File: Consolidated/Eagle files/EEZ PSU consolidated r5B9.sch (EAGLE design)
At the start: 534 parts, among them IC1 LTC3864EMSE#PBF, IC10 REF5025AIDG4, IC11 DAC8552IDGKTG4, IC12 ADG465SOT-23, IC13 TS5A9411DCKT, IC14 ADS1120IPWR, IC15 LP339D, IC16 LM25575MH/NOPB, IC17 TPD4E002DRLR, IC18 TPD2E001DZDR, IC19 ADUM3160BRWZ, IC2 MC79L05, IC20 TLC5925IDBQR, IC21 Si8641EC-B-IS1, IC22 SI8651EC-B-IS1, IC23 SI8651EC-B-IS1, IC24 LD1117ADT33TR, IC25 Si8641EC-B-IS1, IC26 PCA21125T/Q900/1,1, IC27 AT25256B-SSHL-B, IC28 W5500, IC29 BC857BS, IC3 MC78L05, IC30 TLC555, IC31 SN74LVC2G08DCTR, IC32 TPS3705-33D, IC33 SN74LV1T34DBVR, IC34 SN74LVC2G02DCTR, IC4 LM5574MTX/NOPB, IC5 LP2951SO8, IC6 TL072D, IC7 TL072D, IC8 OP27GSZ, IC9 MCP23S08-E/SO, J1 BS-244DSM-R, J2 BS-244DSM-G, J3 BS-244DSM-B, J4 BS-244DSM-R, J5 BS-244DSM-B, Q1 SUD19P06-60, Q10 MMBT5401, Q11 MMBT5401, Q12 MMBT5551, Q13 MMBT5551, Q14 BSS84P, Q15 2N7002, Q16 MMBT5551, Q17 MMBT5401, Q18 MMBT5551, Q19 MMBT5551, Q2 MMBT5401, Q20 BTA26-600, Q21 BTA26-600, Q22 IRLL014N, Q23 IRLML2246TRPBF, Q24 IRLML2246TRPBF, Q25 IRLML2246TRPBF, Q26 IRLML2246TRPBF, Q27 2N7002, Q28 IRLML2246TRPBF, Q29 2N7002, Q3 2N7002, Q30 2N7002, Q4 IRFP250N, Q5 BC857C, Q6 BC846C, Q7 BCP56-16.115, Q8 IRFR5410, Q9 BCP56-16.115, SW1 A101SYCQ04, SW2 1301.9316, X1 39303035, X10 826629-5, X11 2411-01, X12 MC000006, X13 TSW-113-07-F-D, X14 MC000005, X15 TSW-113-07-F-D, X16 09185067324, X17 22-23-2021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

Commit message: C39 marked as n.c.
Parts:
- C39: value 2u2 -> n.c.
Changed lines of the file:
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@@
 <part name="D10" library="EEZ_Lib1" deviceset="SCHOTTKY" device="SOD123" value="DFLS1100-7"/>
 <part name="C31" library="rcl" deviceset="C-EU" device="C1206" value="1u/100V"/>
-<part name="C39" library="rcl" deviceset="C-EU" device="C0805" value="2u2">
+<part name="C39" library="rcl" deviceset="C-EU" device="C0805" value="n.c.">
 <variant name="Farnell" value="2320829"/>
 <variant name="TME" value="CL21B225KAFNNNG "/>

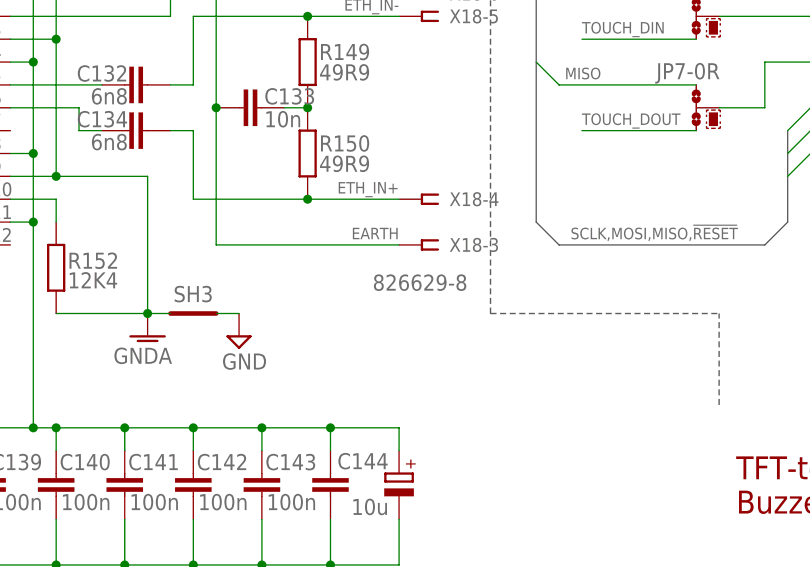
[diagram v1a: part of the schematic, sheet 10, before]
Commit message: X18 type changed
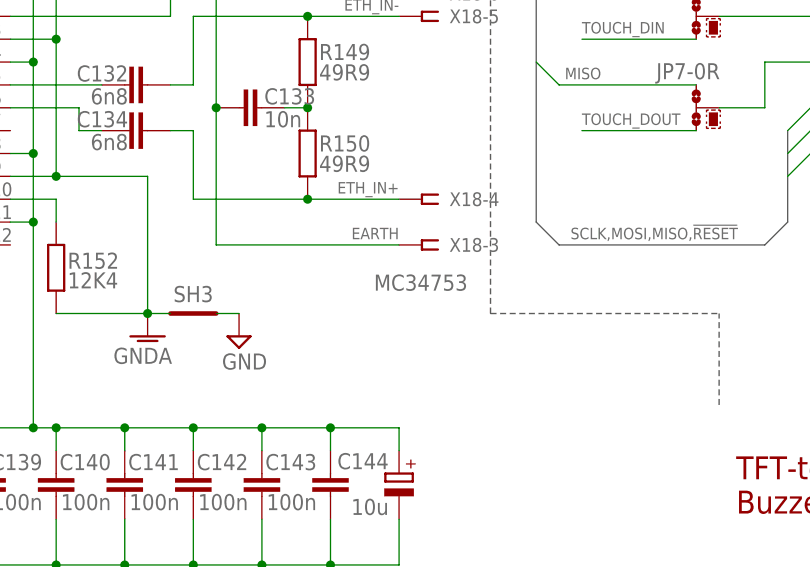
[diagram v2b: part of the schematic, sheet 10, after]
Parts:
- X18: value 826629-8 -> MC34753
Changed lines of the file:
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@@
 <part name="OK3" library="EEZ_Lib1" deviceset="HCPL-181" device=""/>
 <part name="R159" library="rcl" deviceset="R-EU_" device="R0805" value="1K8"/>
-<part name="X18" library="con-samtec" deviceset="SSW-108-02-S-S" device="" value="826629-8">
+<part name="X18" library="con-samtec" deviceset="SSW-108-02-S-S" device="" value="MC34753">
 <attribute name="MPN" value="SSW-108-02-S-S"/>
 <attribute name="OC_NEWARK" value="11P9448"/>

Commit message: R97 and R102 values swapped
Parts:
- R102: value 5K6 -> 4K7
- R97: value 4K7 -> 5K6
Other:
- note added: "+0.275V"
- note added: "+5.18V @ Vout=+5V"
- note added: "+5.19V @ Vout=+5V"
- note added: "-2.72V"
- note removed: "+0.22V"
- note removed: "-2.27V"
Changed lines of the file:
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@@
 <part name="C73" library="rcl" deviceset="C-EU" device="C0603" value="100n"/>
 <part name="FRAME5" library="frames" deviceset="DINA4_L" device=""/>
-<part name="R102" library="rcl" deviceset="R-EU_" device="R0805" value="5K6"/>
+<part name="R102" library="rcl" deviceset="R-EU_" device="R0805" value="4K7"/>
 <part name="R94" library="rcl" deviceset="R-EU_" device="R0805" value="2K2"/>
 <part name="R92" library="rcl" deviceset="R-EU_" device="R0805" value="5K6"/>
@@
 <part name="SUPPLY4" library="supply2" deviceset="GND" device="" value="PGND"/>
 <part name="SUPPLY22" library="supply2" deviceset="GND" device="" value="PGND"/>
-<part name="R97" library="rcl" deviceset="R-EU_" device="R0805" value="4K7"/>
+<part name="R97" library="rcl" deviceset="R-EU_" device="R0805" value="5K6"/>
 <part name="SUPPLY1" library="supply2" deviceset="GND" device="" value="PGND"/>
 <part name="SUPPLY2" library="supply2" deviceset="-9V" device=""/>
@@
 <plain>
 <text x="7.62" y="172.72" size="1.778" layer="97" rot="MR180">Constant Voltage (CV) and Constant Current (CC) mode indicator</text>
-<text x="87.63" y="144.145" size="1.27" layer="100" rot="MR180">+0.22V</text>
+<text x="87.63" y="144.145" size="1.27" layer="100" rot="MR180">+0.275V</text>
 <text x="164.465" y="28.575" size="2.54" layer="94" font="vector">CC/CV indicators, Sense error detection</text>
 <polygon width="0.1524" layer="101">
 </polygon>
-<text x="88.265" y="118.745" size="1.27" layer="100" rot="MR180">-2.27V</text>
+<text x="88.265" y="118.745" size="1.27" layer="100" rot="MR180">-2.72V</text>
 <text x="2.54" y="7.62" size="1.778" layer="94">Licensed under the TAPR Open Hardware License (www.tapr.org/OHL)</text>
 <text x="2.54" y="2.54" size="1.778" layer="94">Repository: https://github.com/eez-open</text>
@@
 <wire x1="7.62" y1="76.835" x2="134.62" y2="76.835" width="0.1524" layer="97" style="shortdash"/>
 <wire x1="134.62" y1="76.835" x2="259.08" y2="76.835" width="0.1524" layer="97" style="shortdash"/>
+<text x="57.15" y="139.065" size="1.27" layer="100" rot="MR180">+5.19V @ Vout=+5V</text>
+<text x="22.225" y="142.875" size="1.27" layer="100" rot="MR180">+5.18V @ Vout=+5V</text>
 </plain>
 <instances>

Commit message: new BOM, added RS and DigiKeyne
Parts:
- C1, C2, C3: value 100n -> 4n7/100V
- C105, C108, C110, C112: value 10n -> 4n7/200V
- C106, C111: value UPW1J150MED -> EEEFK1J220P
- C47, C51: value 1n -> 2n2
- Q1: value SUD19P06-60 -> IRFR5305
- X5: value 09185067324 -> 09185107324
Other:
- note added: "15K / 16K"
- note added: "20K / 22K"
- note added: "Make this correction to enable remote voltage programming!"
- note added: "Note 1.1: Possible alternative AUIRFR5305, SUD19P06-60, SPD30P06P or other with similar or lower input capacitance"
- note added: "Note 1.4: Install 0R only if 100% Duty cycle feature is not needed (do not mount Q3 in that case)"
- note added: "Note 3.2: Place for optional TVS (its primary position is on the Arduino shield board)"
- note added: "R47, R57 / ext.range"
- note removed: "+5.18V @ Vout=+5V"
- note removed: "+5.19V @ Vout=+5V"
- note removed: "15K"
- note removed: "20K"
- note removed: "DC input option"
- note removed: "IRFP250N"
- note removed: "IRFP260N"
- note removed: "Note 1.1: D1-D5, L2 and Q1 requires thermal bridge to the external heatsink. See layer 114 on Board editor for an example."
- note removed: "Note 1.4: Install 0R only if 100% Duty cycle feature is not needed"
- note removed: "Note 3.2: Place for optional TVS (primary place is the Arduino shield board)"
- note removed: "Q4"
- note removed: "R47, R57"
- moved on the sheet: C1, C10, C11, C12, C13, C14, C15, C16, C17, C18, C19, C20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

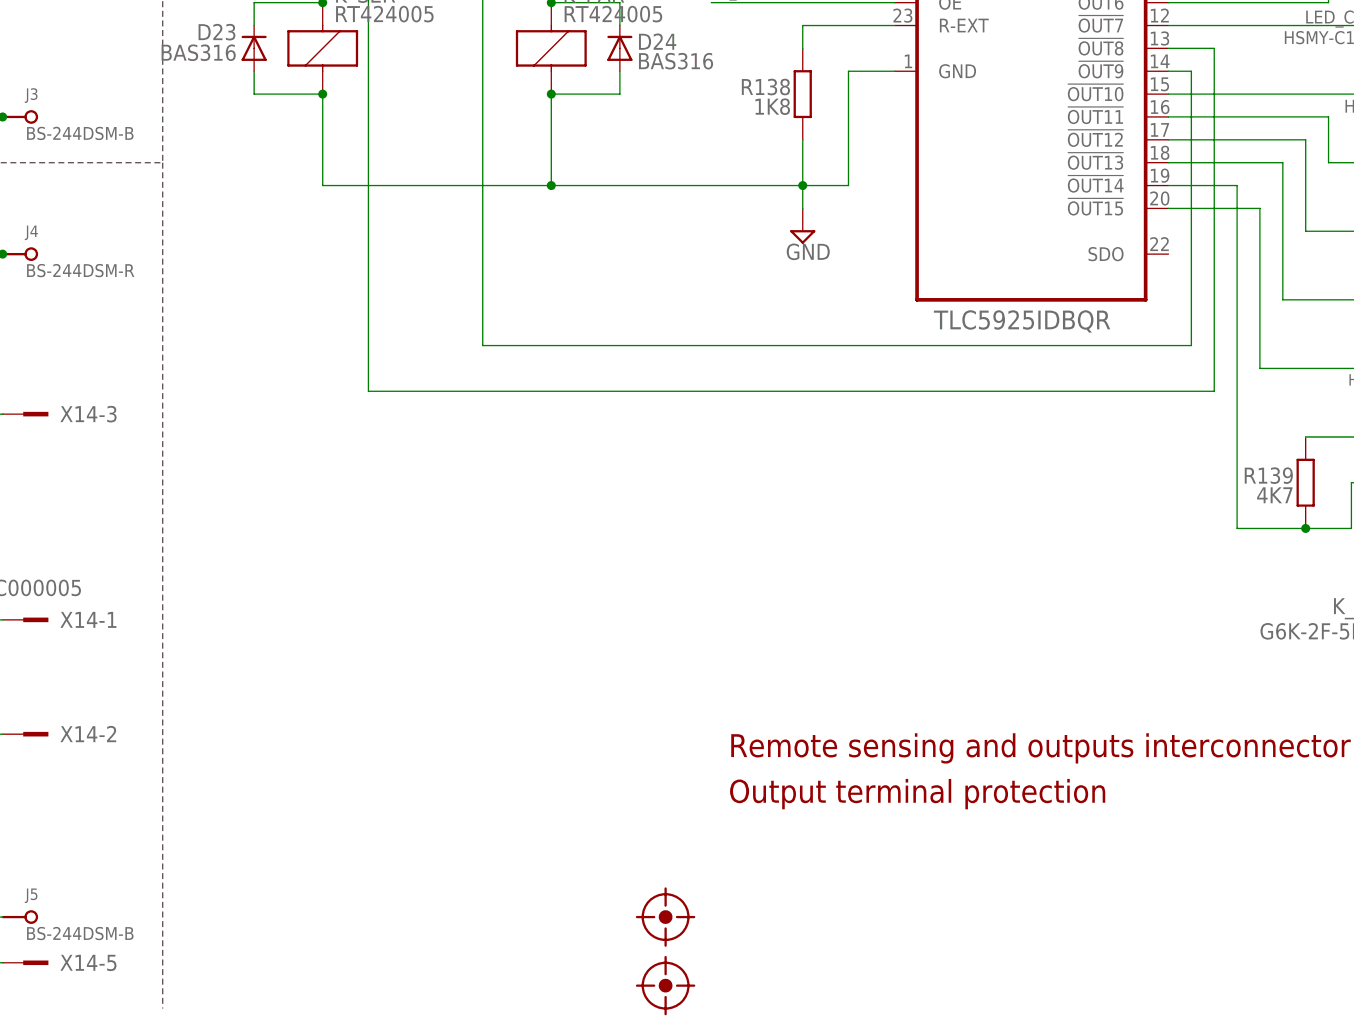
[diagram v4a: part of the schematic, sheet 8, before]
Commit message: Changed wrong designators in schematics on page 3, 6 and 8
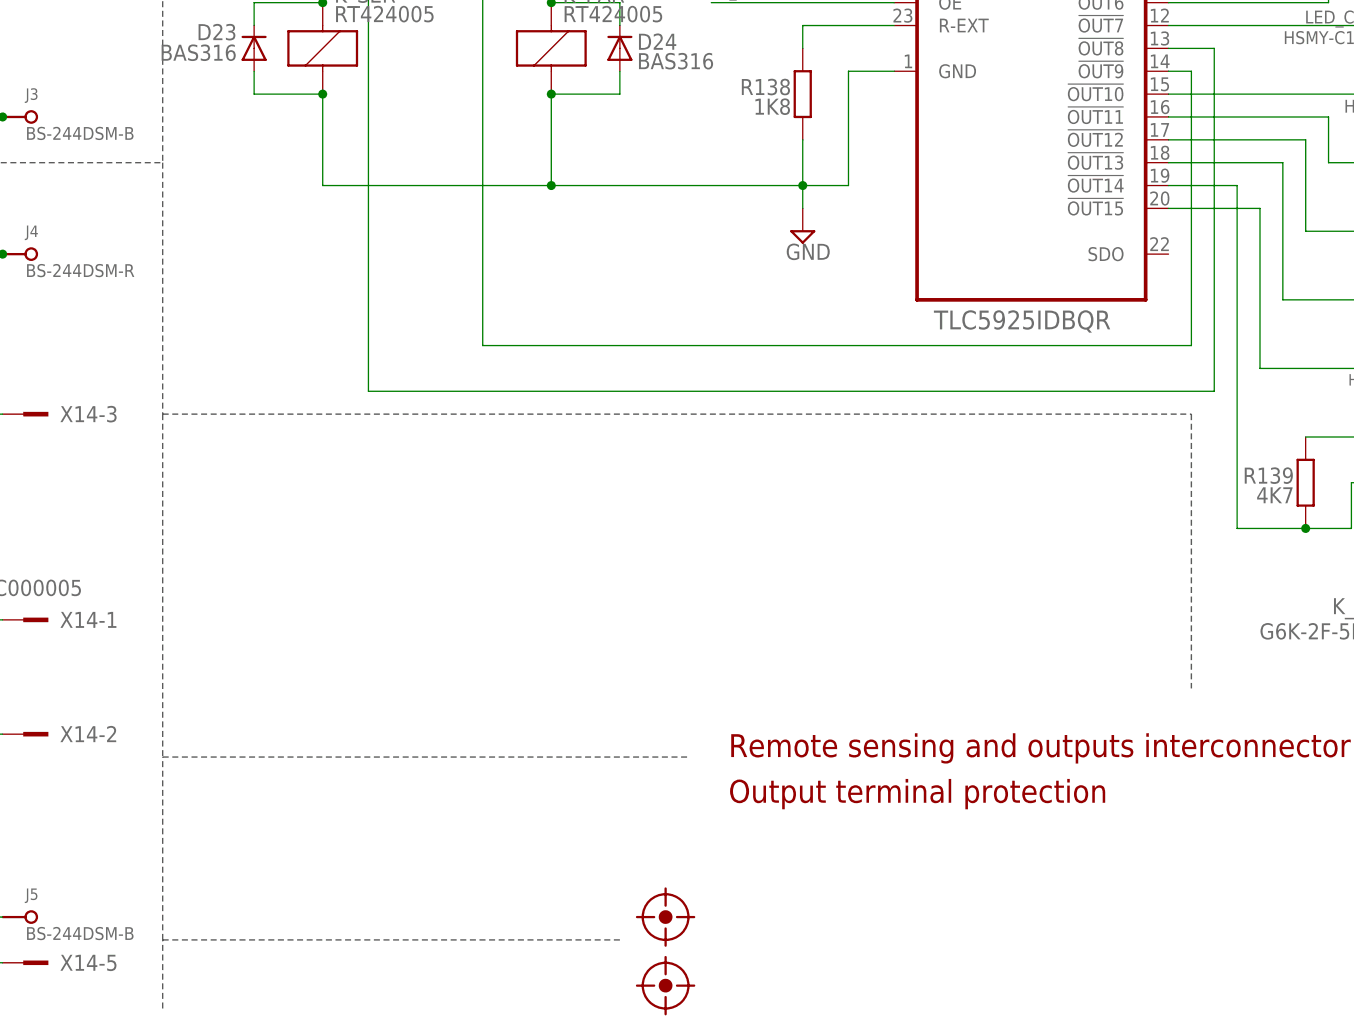
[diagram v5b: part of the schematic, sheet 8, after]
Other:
- note added: "(Rout1, Cout1 and Rout2, Cout2 in BOM)"
- note added: "Note 8.1: Solder X12 and X14 on the PCB's opposite side"
- note added: "R49, R59"
- note added: "R50, R60 / ext.range"
- note added: "R64, R72"
- note added: "Solder 1uF+1R on the channel's outputs"
- note added: "ZD6, ZD7"
- note added: "ZD8, ZD9"
- note removed: "Note 8.1: Solder X1 and X3 on the PCB's opposite side"
- note removed: "R46, R56"
- note removed: "R47, R57 / ext.range"
- note removed: "R61, R69"
- note removed: "ZD1, ZD2"
- note removed: "ZD1-ZD4"
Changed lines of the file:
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@@
 <text x="225.425" y="-53.975" size="1.6764" layer="103">0-40V</text>
 <text x="225.425" y="-56.515" size="1.6764" layer="103">0-50V</text>
-<text x="247.65" y="-48.26" size="1.6764" layer="103">R47, R57 / ext.range</text>
-<text x="234.95" y="-48.26" size="1.6764" layer="103">R46, R56</text>
+<text x="247.65" y="-48.26" size="1.6764" layer="103">R50, R60 / ext.range</text>
+<text x="234.95" y="-48.26" size="1.6764" layer="103">R49, R59</text>
 <text x="238.125" y="-51.435" size="1.6764" layer="103">75K</text>
 <text x="252.73" y="-51.435" size="1.6764" layer="103">15K / 16K</text>
@@
 <text x="224.155" y="-66.675" size="1.6764" layer="103">0-3.12A</text>
 <text x="224.155" y="-69.215" size="1.6764" layer="103">0-4.16A</text>
-<text x="234.95" y="-63.5" size="1.6764" layer="103">R61, R69</text>
+<text x="234.95" y="-63.5" size="1.6764" layer="103">R64, R72</text>
 <text x="238.125" y="-66.675" size="1.6764" layer="103">3K9</text>
 <text x="237.49" y="-69.215" size="1.6764" layer="103">3K24</text>
@@
 <text x="6.985" y="34.925" size="1.6764" layer="103">SAR1</text>
 <text x="6.985" y="19.685" size="1.6764" layer="103">VAR1, VAR2</text>
-<text x="6.985" y="17.145" size="1.6764" layer="103">ZD1, ZD2</text>
+<text x="6.985" y="17.145" size="1.6764" layer="103">ZD6, ZD7</text>
 <text x="44.45" y="38.1" size="1.6764" layer="103">Code</text>
 <text x="24.13" y="38.1" size="1.6764" layer="103">Value</text>
@@
 <text x="3.175" y="91.44" size="1.778" layer="103">Ch#2 Power/Sense</text>
 <wire x1="101.6" y1="175.26" x2="101.6" y2="96.52" width="0.1524" layer="97" style="shortdash"/>
-<wire x1="101.6" y1="96.52" x2="101.6" y2="2.54" width="0.1524" layer="97" style="shortdash"/>
+<wire x1="101.6" y1="96.52" x2="101.6" y2="68.58" width="0.1524" layer="97" style="shortdash"/>
+<wire x1="101.6" y1="68.58" x2="101.6" y2="30.48" width="0.1524" layer="97" style="shortdash"/>
 <wire x1="2.54" y1="96.52" x2="101.6" y2="96.52" width="0.1524" layer="97" style="shortdash"/>
 <text x="189.23" y="82.55" size="1.4224" layer="104">Require SPI_MODE0</text>
 <text x="2.54" y="2.54" size="1.778" layer="94">Licensed under the TAPR Open Hardware License (www.tapr.org/OHL)</text>
-<text x="104.14" y="2.54" size="1.4224" layer="103">Note 8.1: Solder X1 and X3 on the PCB's opposite side</text>
+<text x="104.14" y="33.02" size="1.4224" layer="103">Note 8.1: Solder X12 and X14 on the PCB's opposite side</text>
 <text x="78.74" y="147.32" size="1.4224" layer="103">See Note 8.1</text>
 <text x="76.2" y="66.04" size="1.4224" layer="103">See Note 8.1</text>
@@
 <wire x1="165.1" y1="53.34" x2="172.72" y2="60.96" width="0.1524" layer="101"/>
 <wire x1="172.72" y1="60.96" x2="179.07" y2="60.96" width="0.1524" layer="101"/>
-<text x="106.045" y="14.605" size="1.6764" layer="103">0-30V</text>
-<text x="106.045" y="12.065" size="1.6764" layer="103">0-40V</text>
-<text x="106.045" y="9.525" size="1.6764" layer="103">0-50V</text>
-<text x="116.84" y="17.78" size="1.6764" layer="103">ZD1-ZD4</text>
-<text x="115.57" y="14.605" size="1.6764" layer="103">P4SMAJ36A</text>
-<text x="115.57" y="12.065" size="1.6764" layer="103">P4SMAJ48A</text>
-<text x="115.57" y="9.525" size="1.6764" layer="103">P4SMAJ60A</text>
-<wire x1="104.14" y1="20.32" x2="114.3" y2="20.32" width="0.1524" layer="103"/>
-<wire x1="114.3" y1="20.32" x2="129.54" y2="20.32" width="0.1524" layer="103"/>
-<wire x1="129.54" y1="20.32" x2="129.54" y2="17.145" width="0.1524" layer="103"/>
-<wire x1="129.54" y1="17.145" x2="129.54" y2="8.89" width="0.1524" layer="103"/>
-<wire x1="129.54" y1="8.89" x2="114.3" y2="8.89" width="0.1524" layer="103"/>
-<wire x1="114.3" y1="8.89" x2="104.14" y2="8.89" width="0.1524" layer="103"/>
-<wire x1="104.14" y1="8.89" x2="104.14" y2="17.145" width="0.1524" layer="103"/>
-<wire x1="104.14" y1="17.145" x2="104.14" y2="20.32" width="0.1524" layer="103"/>
-<wire x1="114.3" y1="8.89" x2="114.3" y2="17.145" width="0.1524" layer="103"/>
-<text x="106.045" y="17.78" size="1.6764" layer="103">Range</text>
+<text x="108.585" y="19.685" size="1.6764" layer="103">0-30V</text>
+<text x="108.585" y="17.145" size="1.6764" layer="103">0-40V</text>
+<text x="108.585" y="14.605" size="1.6764" layer="103">0-50V</text>
+<text x="119.38" y="22.86" size="1.6764" layer="103">ZD8, ZD9</text>
+<text x="118.11" y="19.685" size="1.6764" layer="103">P4SMAJ36A</text>
+<text x="118.11" y="17.145" size="1.6764" layer="103">P4SMAJ48A</text>
+<text x="118.11" y="14.605" size="1.6764" layer="103">P4SMAJ60A</text>
+<wire x1="106.68" y1="25.4" x2="116.84" y2="25.4" width="0.1524" layer="103"/>
+<wire x1="116.84" y1="25.4" x2="132.08" y2="25.4" width="0.1524" layer="103"/>
+<wire x1="132.08" y1="25.4" x2="132.08" y2="22.225" width="0.1524" layer="103"/>
+<wire x1="132.08" y1="22.225" x2="132.08" y2="13.97" width="0.1524" layer="103"/>
+<wire x1="132.08" y1="13.97" x2="116.84" y2="13.97" width="0.1524" layer="103"/>
+<wire x1="116.84" y1="13.97" x2="106.68" y2="13.97" width="0.1524" layer="103"/>
+<wire x1="106.68" y1="13.97" x2="106.68" y2="22.225" width="0.1524" layer="103"/>
+<wire x1="106.68" y1="22.225" x2="106.68" y2="25.4" width="0.1524" layer="103"/>
+<wire x1="116.84" y1="13.97" x2="116.84" y2="22.225" width="0.1524" layer="103"/>
+<text x="108.585" y="22.86" size="1.6764" layer="103">Range</text>
 <text x="27.94" y="126.365" size="1.4224" layer="103">See Table 1</text>
 <text x="27.94" y="38.1" size="1.4224" layer="103">See Table 1</text>
-<text x="104.14" y="21.59" size="1.4224" layer="103">Table 1</text>
-<wire x1="114.3" y1="17.145" x2="114.3" y2="20.32" width="0.1524" layer="103"/>
-<wire x1="129.54" y1="17.145" x2="114.3" y2="17.145" width="0.1524" layer="103"/>
-<wire x1="104.14" y1="17.145" x2="114.3" y2="17.145" width="0.1524" layer="103"/>
+<text x="106.68" y="26.67" size="1.4224" layer="103">Table 1</text>
+<wire x1="116.84" y1="22.225" x2="116.84" y2="25.4" width="0.1524" layer="103"/>
+<wire x1="132.08" y1="22.225" x2="116.84" y2="22.225" width="0.1524" layer="103"/>
+<wire x1="106.68" y1="22.225" x2="116.84" y2="22.225" width="0.1524" layer="103"/>
 <rectangle x1="65.405" y1="136.525" x2="71.12" y2="143.51" layer="97"/>
 <rectangle x1="65.405" y1="122.555" x2="71.755" y2="128.27" layer="97"/>
 <rectangle x1="65.405" y1="52.705" x2="71.755" y2="59.69" layer="97"/>
 <rectangle x1="65.405" y1="36.195" x2="71.755" y2="42.545" layer="97"/>
+<wire x1="101.6" y1="30.48" x2="160.02" y2="30.48" width="0.1524" layer="97" style="shortdash"/>
+<wire x1="101.6" y1="2.54" x2="101.6" y2="10.16" width="0.1524" layer="97" style="shortdash"/>
+<wire x1="101.6" y1="10.16" x2="101.6" y2="30.48" width="0.1524" layer="97" style="shortdash"/>
+<wire x1="101.6" y1="68.58" x2="215.9" y2="68.58" width="0.1524" layer="97" style="shortdash"/>
+<wire x1="215.9" y1="68.58" x2="215.9" y2="38.1" width="0.1524" layer="97" style="shortdash"/>
+<wire x1="101.6" y1="10.16" x2="152.4" y2="10.16" width="0.1524" layer="97" style="shortdash"/>
+<text x="104.14" y="5.08" size="1.4224" layer="103">Solder 1uF+1R on the channel's outputs</text>
+<text x="104.14" y="2.54" size="1.4224" layer="103">(Rout1, Cout1 and Rout2, Cout2 in BOM)</text>
 </plain>
 <instances>
